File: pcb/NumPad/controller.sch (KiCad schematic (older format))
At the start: 31 parts, among them IC1 IS31FL3731, J1 USB_OTG, J2 ISP, J3 GS2, J4 GS2, J5 GS2, J6 GS2, J7 Conn_01x06, U1 ATmega32U4, Y1 Crystal

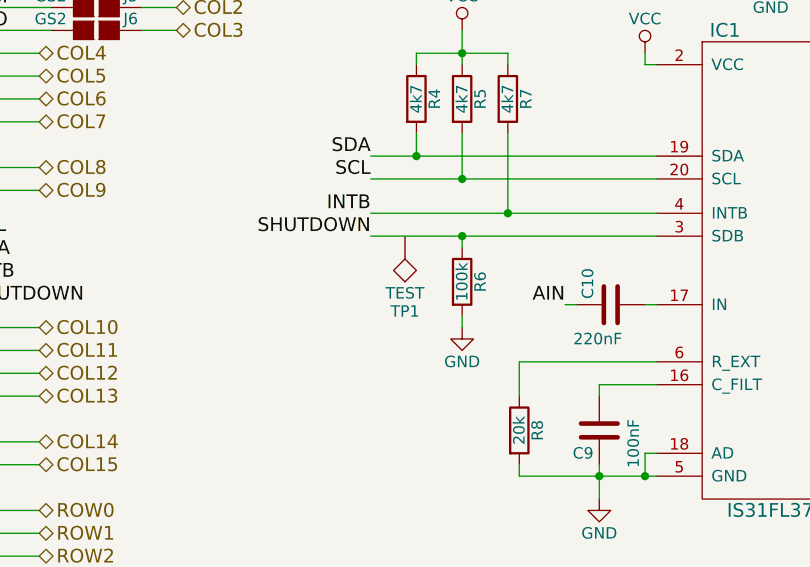
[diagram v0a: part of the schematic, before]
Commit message: changes in Numpad
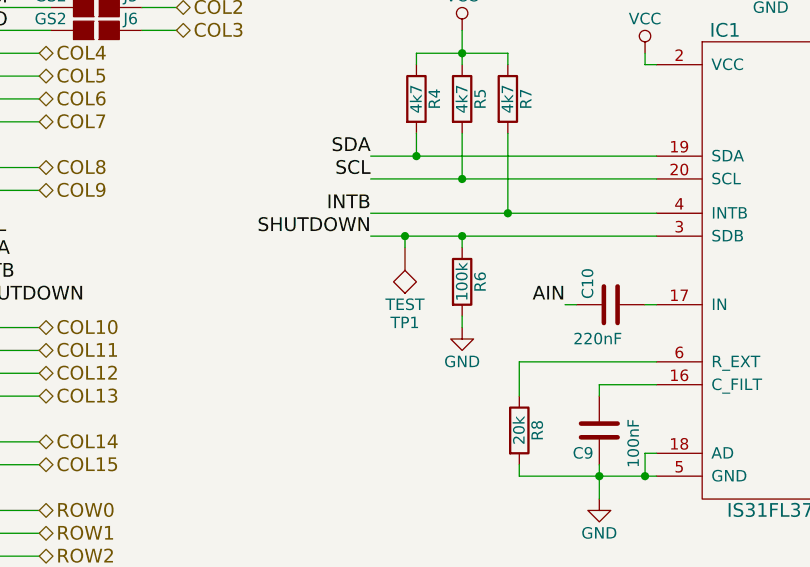
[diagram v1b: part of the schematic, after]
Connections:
- net SHUTDOWN: now also TP1.1
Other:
- moved on the sheet: TP1
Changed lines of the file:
@@
 L TEST TP1
 U 1 1 5ABC0ACE
-P 6550 2750
-F 0 "TP1" H 6550 3050 50  0000 C BNN
-F 1 "TEST" H 6550 3000 50  0000 C CNN
-F 2 "Pin_Headers:Pin_Header_Straight_1x01_Pitch2.54mm" H 6550 2750 50  0001 C CNN
-F 3 "" H 6550 2750 50  0001 C CNN
-	1    6550 2750
+P 6550 2800
+F 0 "TP1" H 6550 3100 50  0000 C BNN
+F 1 "TEST" H 6550 3050 50  0000 C CNN
+F 2 "Pin_Headers:Pin_Header_Straight_1x01_Pitch2.54mm" H 6550 2800 50  0001 C CNN
+F 3 "" H 6550 2800 50  0001 C CNN
+	1    6550 2800
 	-1   0    0    1
 $EndComp
@@
 Text Notes 650  600  0    60   ~ 0
 Micro USB: 10118194-0001LF (Amphenol), Digikey: 609-4618-1-ND
+Wire Wire Line
+	6550 2800 6550 2750
+Connection ~ 6550 2750
 $EndSCHEMATC

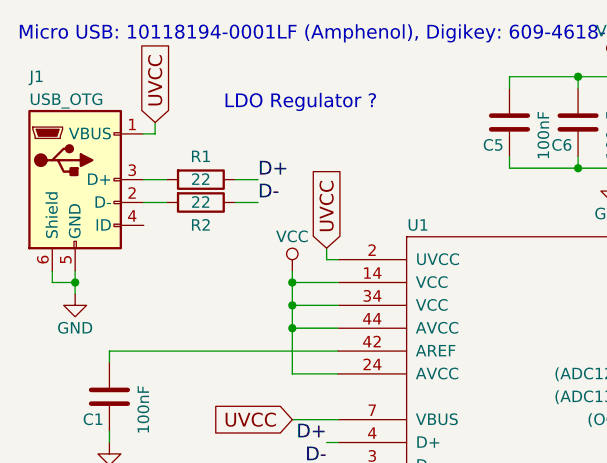
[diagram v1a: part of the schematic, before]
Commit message: changes in NumPad layout
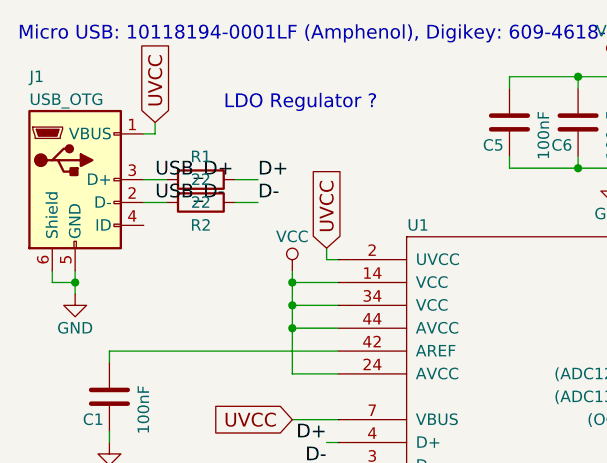
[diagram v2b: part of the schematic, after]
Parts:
- J2: footprint Pin_Headers:Pin_Header_Straight_2x03_Pitch2.54mm -> Pin_Headers:Pin_Header_Straight_1x06_Pitch2.54mm
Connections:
- net USB_D-: now reaches J1.2 (D-), R2.2
- net USB_D+: now reaches J1.3 (D+), R1.2
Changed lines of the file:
@@
 F 0 "J2" H 3250 5300 50  0000 C CNN
 F 1 "ISP" H 3250 4900 50  0000 C CNN
-F 2 "Pin_Headers:Pin_Header_Straight_2x03_Pitch2.54mm" H 3200 5100 50  0001 C CNN
+F 2 "Pin_Headers:Pin_Header_Straight_1x06_Pitch2.54mm" H 3200 5100 50  0001 C CNN
 F 3 "" H 3200 5100 50  0001 C CNN
 	1    3200 5100
@@
 	6550 2800 6550 2750
 Connection ~ 6550 2750
+Text Label 1250 1200 0    60   ~ 0
+USB_D+
+Text Label 1250 1300 0    60   ~ 0
+USB_D-
 $EndSCHEMATC
